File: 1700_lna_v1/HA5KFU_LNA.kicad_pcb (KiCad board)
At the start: 2 copper layers, 26.7 x 17.8 mm, 17 parts, among them J1 Conn_Coaxial, J2 Conn_Coaxial, J3 Conn_01x02_Socket, U1 NCP163ASN330T1G, U2 QPL9547, U3 TFS1690

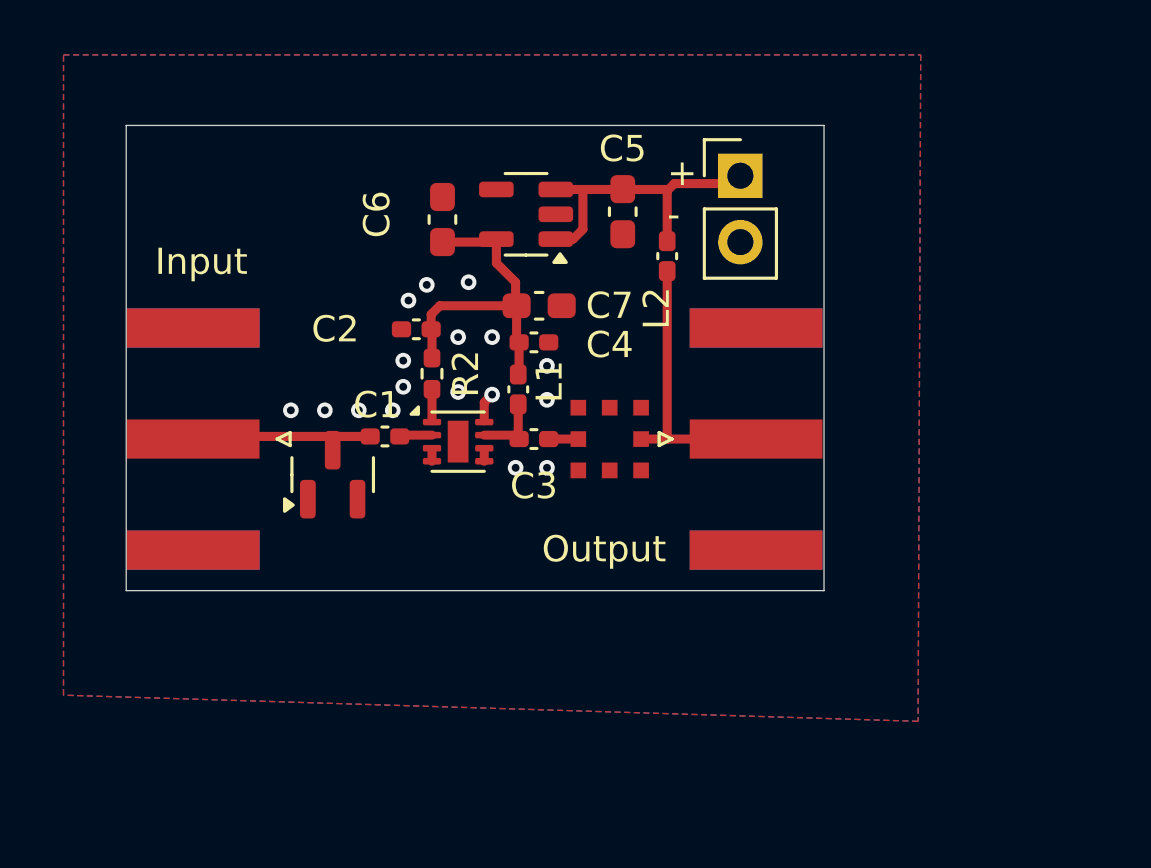
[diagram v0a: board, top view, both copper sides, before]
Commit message: Added BOM, project file
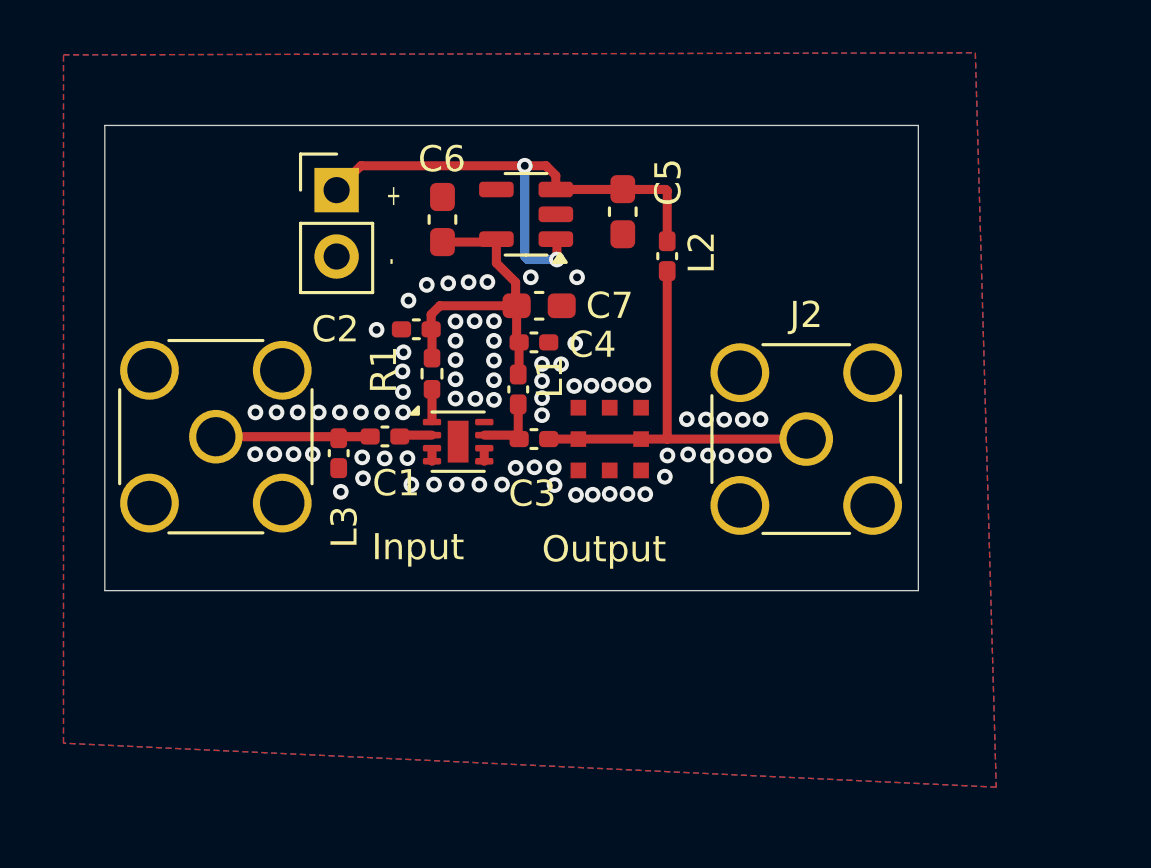
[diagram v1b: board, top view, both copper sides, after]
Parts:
- removed D1: BAT54S, Package_TO_SOT_SMD:SOT-23
- added L3: 33nH, Inductor_SMD:L_0402_1005Metric_Pad0.77x0.64mm_HandSolder, F.Cu at (115.7, 88.8)
- J1: footprint Connector_Coaxial:SMA_Amphenol_132289_EdgeMount -> Connector_Coaxial:SMA_Amphenol_132134_Vertical
- J2: footprint Connector_Coaxial:SMA_Amphenol_132289_EdgeMount -> Connector_Coaxial:SMA_Amphenol_132291_Vertical
- moved J3 15.5 mm to (115.7, 78.8)
- moved J2 1.92 mm to (133.6, 88.3)
- moved J1 0.87 mm to (111.0, 88.2)
- renumbered R2 to R1
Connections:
- C3 pad 2: Net-(U3-In) -> /LNA_OUT
- U3 pad 2: Net-(U3-In) -> /LNA_OUT
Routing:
- net +5V: track 11.6 -> 21.8 mm, vias 0 -> 2
- net /LNA_OUT: track 11.3 -> 16.3 mm
- net Net-(U3-In): track 1.13 -> 0.00 mm
- net GND: track 2.03 -> 0.90 mm, vias 17 -> 77
- net Net-(J1-In): track 7.16 -> 6.06 mm
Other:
- board size 26.7 x 17.8 mm -> 31.1 x 17.8 mm

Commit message: Adjusted 2 layer PCB design
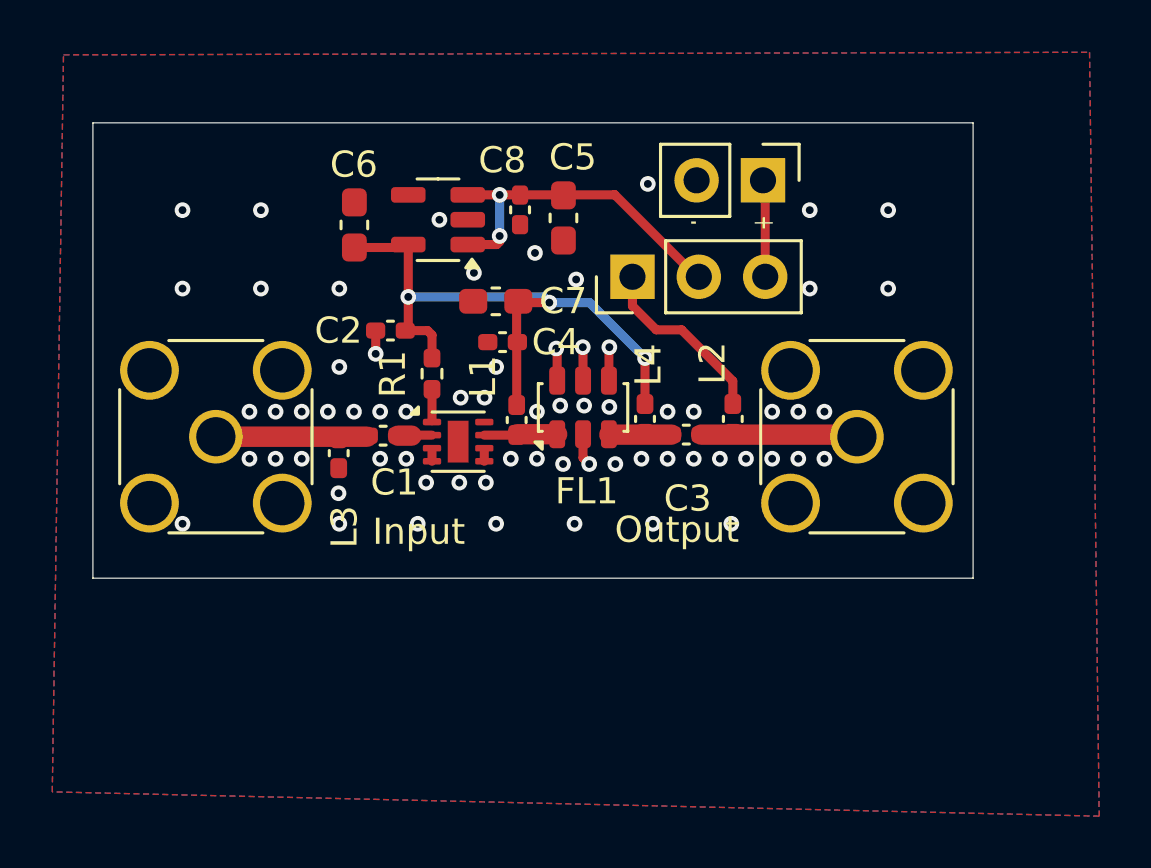
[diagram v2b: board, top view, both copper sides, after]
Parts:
- removed U3: TFS1690, SAW_filt_lib:TFS1690
- added C8: 100pF, Capacitor_SMD:C_0402_1005Metric_Pad0.74x0.62mm_HandSolder, F.Cu at (122.7, 79.5)
- added FL1: BFCN-1690, Filter:Filter_Mini-Circuits_FV1206-1, F.Cu at (125.1, 87.1)
- added J4: Conn_01x03_Socket, Connector_PinHeader_2.54mm:PinHeader_1x03_P2.54mm_Vertical, F.Cu at (127.0, 82.1)
- added L4: 33nH, Inductor_SMD:L_0402_1005Metric_Pad0.77x0.64mm_HandSolder, F.Cu at (127.5, 87.5)
- J2: footprint Connector_Coaxial:SMA_Amphenol_132291_Vertical -> Connector_Coaxial:SMA_Amphenol_132134_Vertical
- moved J3 16.3 mm to (132.0, 78.4), turned to -90 degrees
- moved L2 6.72 mm to (130.8, 87.5)
- moved C3 5.83 mm to (129.0, 88.1)
- moved C6 3.38 mm to (116.3, 80.1)
- moved U1 3.38 mm to (119.5, 79.9)
- moved C5 2.28 mm to (124.3, 79.8)
- moved J2 1.94 mm to (135.6, 88.2)
- moved C7 1.67 mm to (121.7, 83.0), turned to 180 degrees
- moved C4 1.20 mm to (122.0, 84.6), turned to 180 degrees
- moved L1 1.17 mm to (122.5, 87.6)
- moved C2 0.99 mm to (117.7, 84.2)
- moved C1 0.08 mm to (117.4, 88.2)
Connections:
- C3 pad 1: Net-(C3-Pad1) -> Net-(FL1-OUT)
- C5 pad 1: +5V -> Net-(J4-Pin_2)
- L1 pad 2: Net-(C3-Pad1) -> Net-(FL1-IN)
- L2 pad 2: +5V -> Net-(J4-Pin_1)
- U1 pad 1: +5V -> Net-(J4-Pin_2)
- U1 pad 3: +5V -> Net-(J4-Pin_2)
- U2 pad 7: Net-(C3-Pad1) -> Net-(FL1-IN)
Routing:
- net +5V: track 21.8 -> 3.73 mm, vias 2 -> 0
- net Net-(J4-Pin_2): track 0.00 -> 13.3 mm, vias 0 -> 2
- net +3V3: track 12.8 -> 24.4 mm, vias 0 -> 3
- net /LNA_OUT: track 16.3 -> 6.12 mm
- net Net-(J4-Pin_1): track 0.00 -> 7.03 mm
- net GND: track 0.90 -> 6.85 mm, vias 77 -> 67
- net Net-(FL1-IN): track 0.00 -> 2.77 mm
- net Net-(C3-Pad1): track 2.74 -> 0.00 mm
- net Net-(FL1-OUT): track 0.00 -> 2.40 mm
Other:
- board size 31.1 x 17.8 mm -> 33.7 x 17.4 mm
